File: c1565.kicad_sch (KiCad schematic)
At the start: 7 parts, among them J16 MD-90SM, U12 74LS125, U13 74LS125

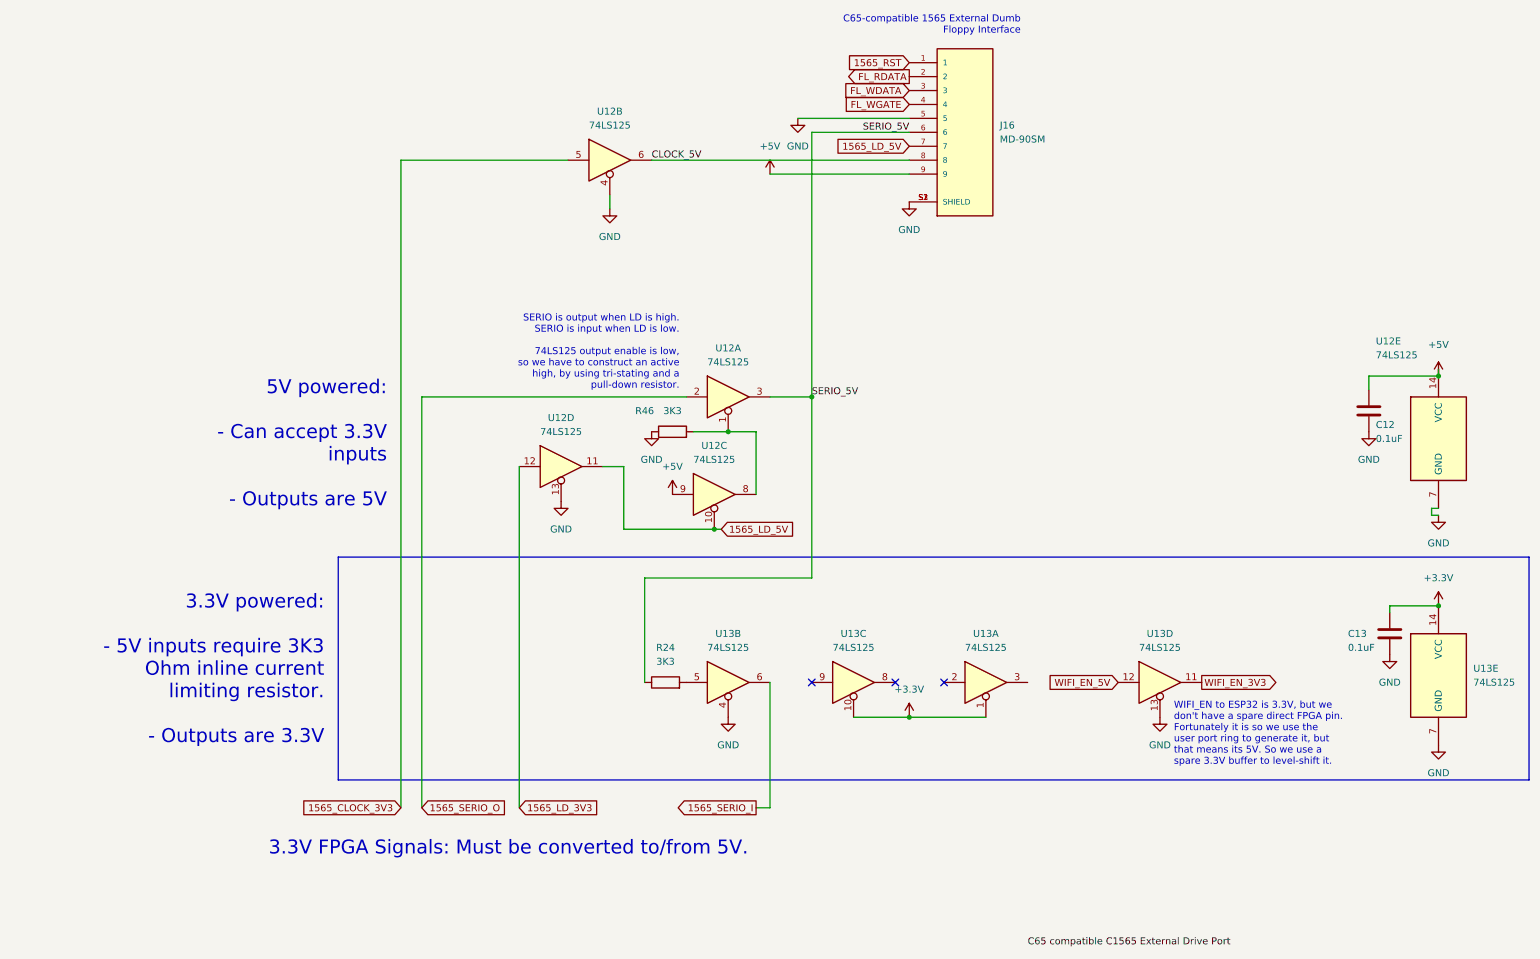
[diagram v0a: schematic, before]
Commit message: Remove everything not needed for JTAG loader board testing
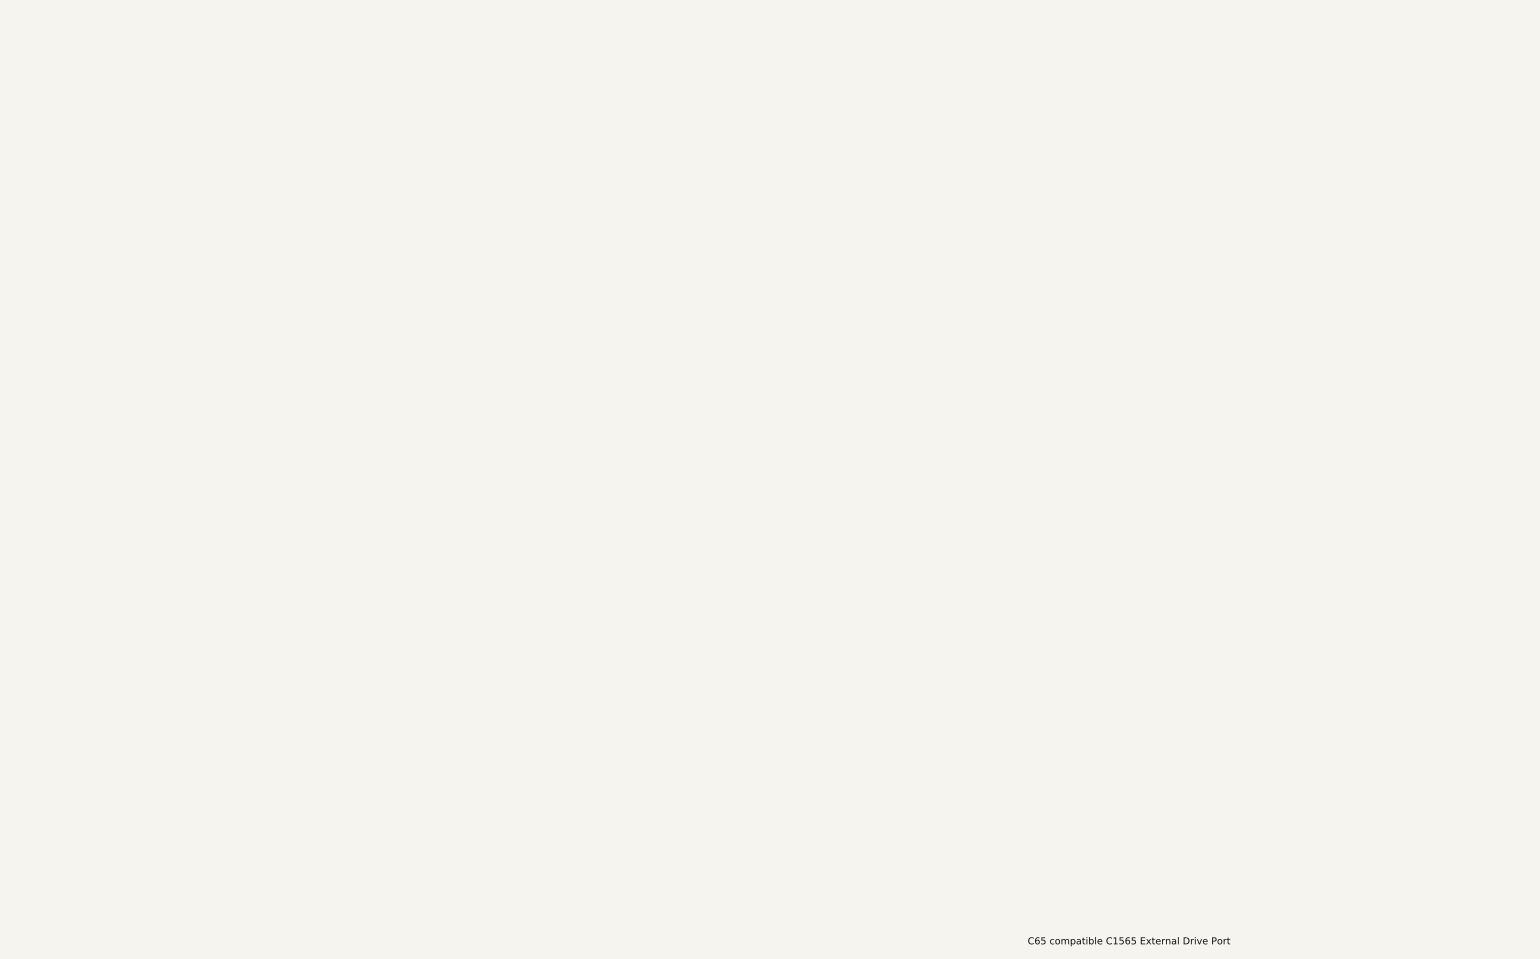
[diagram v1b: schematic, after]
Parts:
- removed C12, C13: 0.1uF, Capacitor_THT:C_Disc_D5.0mm_W2.5mm_P5.00mm, symbol Device:C
- removed J16: MD-90SM, snapeda:CUI_MD-90SM, symbol 00Project-MD90:MD-90SM
- removed R24, R46: 3K3, snapeda:Labeled Resistor, symbol Device:R
- removed U12: 74LS125, snapeda:DIP-14_W7.62mm, symbol 74xx:74LS125
- removed U13: 74LS125, snapeda:DIP-14_74LS06, symbol 74xx:74LS125
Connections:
- no-connect marks 3 -> 0
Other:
- note removed: "3.3V FPGA Signals: Must be converted to/from 5V."
- note removed: "3.3V powered: - 5V inputs require 3K3 Ohm inline current limiting resistor. - Outputs are 3.3V"
- note removed: "5V powered: - Can accept 3.3V inputs - Outputs are 5V"
- note removed: "C65-compatible 1565 External Dumb Floppy Interface"
- note removed: "SERIO is output when LD is high. SERIO is input when LD is low. 74LS125 output enable is low, so we have to construct an active high, by using tri-stating and a pull-down resistor."
- note removed: "WIFI_EN to ESP32 is 3.3V, but we don't have a spare direct FPGA pin. Fortunately it is so we use the user port ring to generate it, but that means its 5V. So we use a spare 3.3V buffer to level-shift it."
